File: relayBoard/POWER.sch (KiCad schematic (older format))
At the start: 22 parts

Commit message: First pass layout finished
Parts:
- removed T?: Transformer_1P_1S, symbol Device:Transformer_1P_1S
- added T1: 750313457, EP10_SMD_H_8PIN_(6052), symbol 750313442:750313442
- C47, C48, C49, C50, C51, C52: renamed from C?; footprint (none) -> Resistor_SMD:R_0603_1608Metric
- C53: renamed from C?; footprint (none) -> Resistor_SMD:R_1210_3225Metric
- D148: renamed from D?; value D_Zener -> CMZ5934B; footprint (none) -> Diode_SMD:D_SMA
- D149: renamed from D?; value D_Schottky -> DFLS1100; footprint (none) -> Diode_SMD:D_PowerDI-123
- D150: renamed from D?; footprint (none) -> Diode_SMD:D_0805_2012Metric
- D151: renamed from D?; value D_Schottky -> PDS360; footprint (none) -> Diode_SMD:D_PowerDI-5
- Q43: renamed from Q?; footprint (none) -> Package_TO_SOT_SMD:Infineon_PG-TO-220-7Lead_TabPin8; symbol Device:Q_NJFET_GSD -> Device:Q_NJFET_GSD_copy
- R173: renamed from R?; value 115k -> R; footprint (none) -> Resistor_SMD:R_0603_1608Metric
- R174: renamed from R?; value 154k -> 121k; footprint (none) -> Resistor_SMD:R_0603_1608Metric
- R175, R176, R177, R178: renamed from R?; footprint (none) -> Resistor_SMD:R_0603_1608Metric
- U5: renamed from U?; footprint (none) -> Package_TO_SOT_SMD:SOT-223-3_TabPin2
- gave numbers to parts that had none: 2
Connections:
- net labels added: HV_OUT
- wire segments 94 -> 99

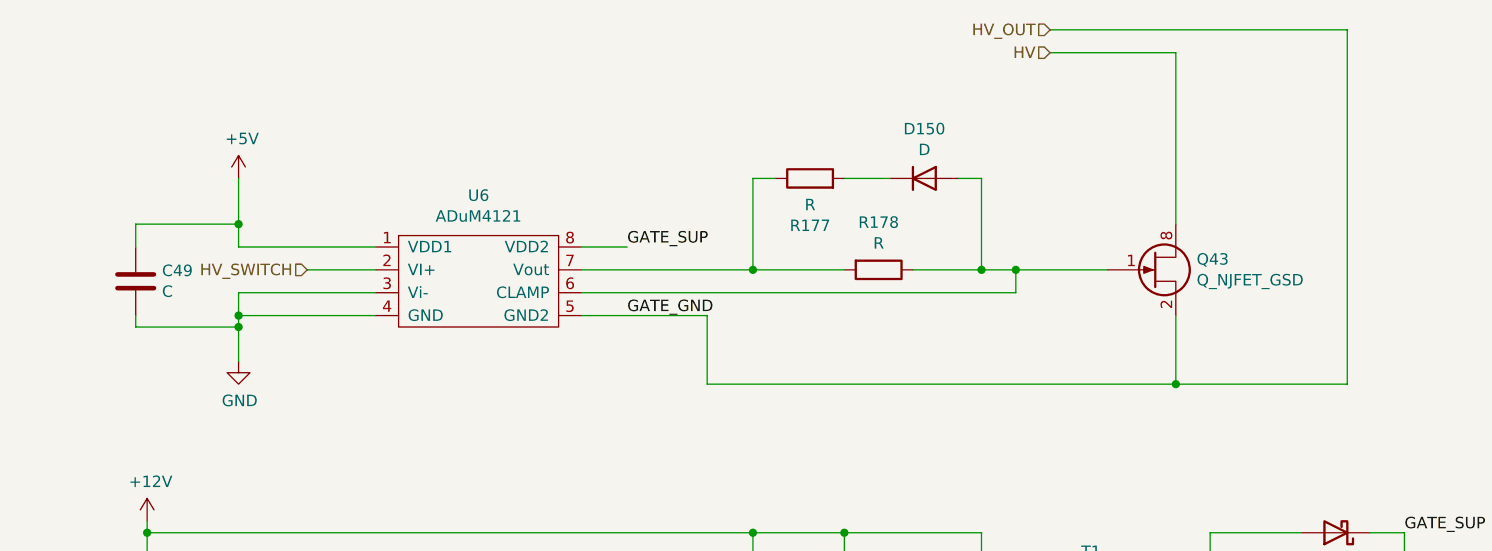
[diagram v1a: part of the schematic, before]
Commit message: Third pass, fixing footprints to match JLC components
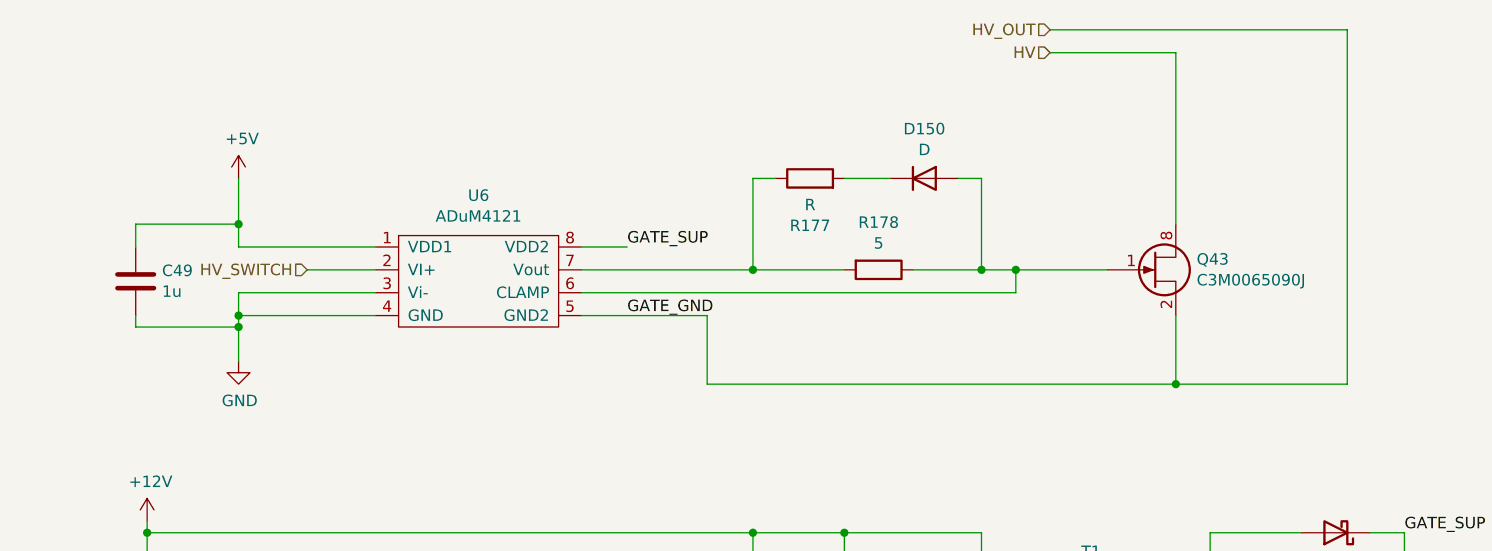
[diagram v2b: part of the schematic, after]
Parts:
- C49: value C -> 1u
- Q43: value Q_NJFET_GSD -> C3M0065090J
- R178: value R -> 5
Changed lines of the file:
@@
 P 3850 2500
 F 0 "C49" H 3965 2546 50  0000 L CNN
-F 1 "C" H 3965 2455 50  0000 L CNN
+F 1 "1u" H 3965 2455 50  0000 L CNN
 F 2 "Resistor_SMD:R_0603_1608Metric" H 3888 2350 50  0001 C CNN
 F 3 "~" H 3850 2500 50  0001 C CNN
@@
 P 7100 2450
 F 0 "R178" V 6893 2450 50  0000 C CNN
-F 1 "R" V 6984 2450 50  0000 C CNN
+F 1 "5" V 6984 2450 50  0000 C CNN
 F 2 "Resistor_SMD:R_0603_1608Metric" V 7030 2450 50  0001 C CNN
 F 3 "~" H 7100 2450 50  0001 C CNN
@@
 P 8300 2450
 F 0 "Q43" H 8491 2496 50  0000 L CNN
-F 1 "Q_NJFET_GSD" H 8491 2405 50  0000 L CNN
+F 1 "C3M0065090J" H 8491 2405 50  0000 L CNN
 F 2 "Package_TO_SOT_SMD:Infineon_PG-TO-220-7Lead_TabPin8" H 8500 2550 50  0001 C CNN
 F 3 "~" H 8300 2450 50  0001 C CNN

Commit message: Cuyler's revisions to the relay board
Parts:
- Q43: symbol Device:Q_NJFET_GSD_copy -> relayBoard-rescue:Q_NJFET_GSD_copy-Device
- T1: symbol 750313442:750313442 -> relayBoard-rescue:750313442-750313442
- U6: symbol adum4121:ADuM4121 -> relayBoard-rescue:ADuM4121-adum4121
- U7: symbol LT8302:LT8302 -> relayBoard-rescue:LT8302-LT8302
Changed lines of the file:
@@
 EESchema Schematic File Version 4
-EELAYER 30 0
+LIBS:relayBoard-cache
+EELAYER 29 0
 EELAYER END
 $Descr A4 11693 8268
@@
 $EndDescr
 $Comp
-L adum4121:ADuM4121 U6
+L relayBoard-rescue:ADuM4121-adum4121 U6
 U 1 1 63138DA1
 P 5300 2600
@@
 $EndComp
 $Comp
-L LT8302:LT8302 U7
+L relayBoard-rescue:LT8302-LT8302 U7
 U 1 1 631398F8
 P 5400 4350
@@
 GATE_GND
 $Comp
-L Device:Q_NJFET_GSD_copy Q43
+L relayBoard-rescue:Q_NJFET_GSD_copy-Device Q43
 U 1 1 631B6EF9
 P 8300 2450
@@
 HV
 $Comp
-L 750313442:750313442 T1
+L relayBoard-rescue:750313442-750313442 T1
 U 1 1 5F3AB14D
 P 8000 4200

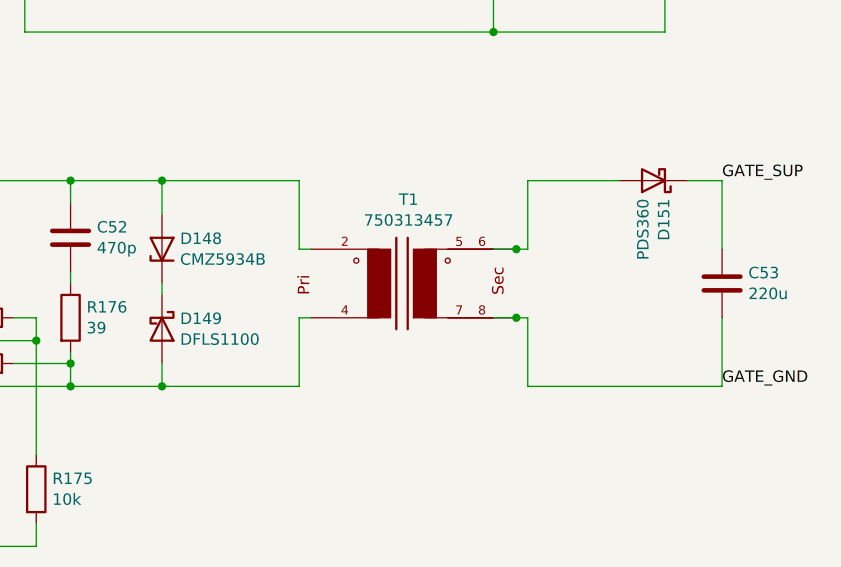
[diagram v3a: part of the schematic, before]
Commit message: updates to connector connections and converter transformer
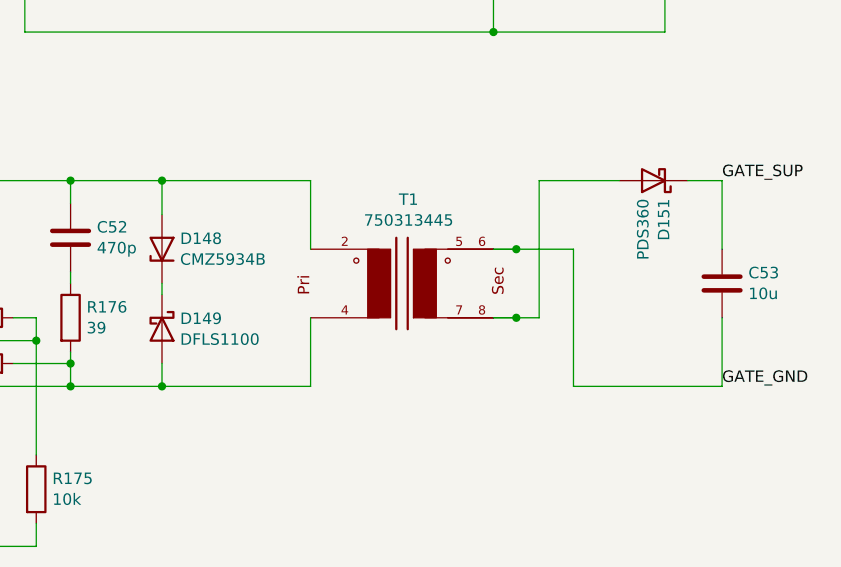
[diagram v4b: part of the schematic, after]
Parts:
- C53: value 220u -> 10u
- T1: value 750313457 -> 750313445
- U6: footprint Package_SO:SOIC-8_5.23x5.23mm_P1.27mm -> Package_SO:SOIC-8_7.5x5.85mm_P1.27mm
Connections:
- net HV_OUT: now also T1.5, T1.6; no longer T1.7, T1.8
- new net: D151.2 (A), T1.7, T1.8
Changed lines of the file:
@@
 EESchema Schematic File Version 4
-LIBS:relayBoard-cache
-EELAYER 29 0
+EELAYER 30 0
 EELAYER END
 $Descr A4 11693 8268
@@
 F 0 "U6" H 5350 3075 50  0000 C CNN
 F 1 "ADuM4121" H 5350 2984 50  0000 C CNN
-F 2 "Package_SO:SOIC-8_5.23x5.23mm_P1.27mm" H 5300 2600 50  0001 C CNN
+F 2 "Package_SO:SOIC-8_7.5x5.85mm_P1.27mm" H 5300 2600 50  0001 C CNN
 F 3 "" H 5300 2600 50  0001 C CNN
 	1    5300 2600
@@
 Wire Wire Line
 	6550 4050 6550 4000
-Wire Wire Line
-	6950 4500 7550 4500
 Connection ~ 6950 4500
-Wire Wire Line
-	7550 3600 6950 3600
 Connection ~ 6950 3600
-Wire Wire Line
-	8550 3600 8950 3600
 $Comp
 L Device:D_Schottky D151
@@
 P 9400 4050
 F 0 "C53" H 9515 4096 50  0000 L CNN
-F 1 "220u" H 9515 4005 50  0000 L CNN
+F 1 "10u" H 9515 4005 50  0000 L CNN
 F 2 "Resistor_SMD:R_1210_3225Metric" H 9438 3900 50  0001 C CNN
 F 3 "~" H 9400 4050 50  0001 C CNN
@@
 	1    0    0    -1
 $EndComp
-Wire Wire Line
-	9400 3600 9250 3600
-Wire Wire Line
-	9400 3600 9400 3900
-Wire Wire Line
-	8550 4500 9400 4500
-Wire Wire Line
-	9400 4500 9400 4200
 Text Label 9400 3600 0    50   ~ 0
 GATE_SUP
@@
 Text HLabel 7850 1500 0    50   Input ~ 0
 HV
+Text HLabel 7850 1400 0    50   Input ~ 0
+HV_OUT
+Wire Wire Line
+	8400 2950 9150 2950
+Wire Wire Line
+	9150 2950 9150 1400
+Wire Wire Line
+	9150 1400 7850 1400
+Connection ~ 8400 2950
+Wire Wire Line
+	8400 4200 8500 4200
+Wire Wire Line
+	7600 3600 7600 3900
+Wire Wire Line
+	6950 3600 7600 3600
+Wire Wire Line
+	7600 4500 7600 4200
+Wire Wire Line
+	6950 4500 7600 4500
+Wire Wire Line
+	9400 3600 9250 3600
+Wire Wire Line
+	9400 3600 9400 3900
+Wire Wire Line
+	9400 4500 9400 4200
+Wire Wire Line
+	8400 3900 8500 3900
 $Comp
 L relayBoard-rescue:750313442-750313442 T1
@@
 P 8000 4200
 F 0 "T1" H 8029 4717 50  0000 C CNN
-F 1 "750313457" H 8029 4626 50  0000 C CNN
+F 1 "750313445" H 8029 4626 50  0000 C CNN
 F 2 "EP10_SMD_H_8PIN_(6052)" H 8000 4200 50  0001 L BNN
 F 3 "" H 8000 4200 50  0001 C CNN
@@
 $EndComp
 Wire Wire Line
-	7550 3900 7600 3900
-Wire Wire Line
-	7550 3600 7550 3900
-Wire Wire Line
-	7550 4200 7600 4200
-Wire Wire Line
-	7550 4200 7550 4500
-Wire Wire Line
-	8550 4200 8550 4500
-Wire Wire Line
-	8550 3600 8550 3900
-Wire Wire Line
-	8400 3900 8500 3900
+	8500 3900 8750 3900
+Wire Wire Line
+	8750 3900 8750 4500
 Connection ~ 8500 3900
 Wire Wire Line
-	8500 3900 8550 3900
-Wire Wire Line
-	8400 4200 8500 4200
+	8750 4500 9400 4500
+Wire Wire Line
+	8600 4200 8500 4200
 Connection ~ 8500 4200
 Wire Wire Line
-	8500 4200 8550 4200
-Text HLabel 7850 1400 0    50   Input ~ 0
-HV_OUT
-Wire Wire Line
-	8400 2950 9150 2950
-Wire Wire Line
-	9150 2950 9150 1400
-Wire Wire Line
-	9150 1400 7850 1400
-Connection ~ 8400 2950
+	8600 3600 8600 4200
+Wire Wire Line
+	8600 3600 8950 3600
 $EndSCHEMATC
